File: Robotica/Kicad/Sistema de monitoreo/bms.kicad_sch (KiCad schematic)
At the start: 3 parts, among them J2 TP4056

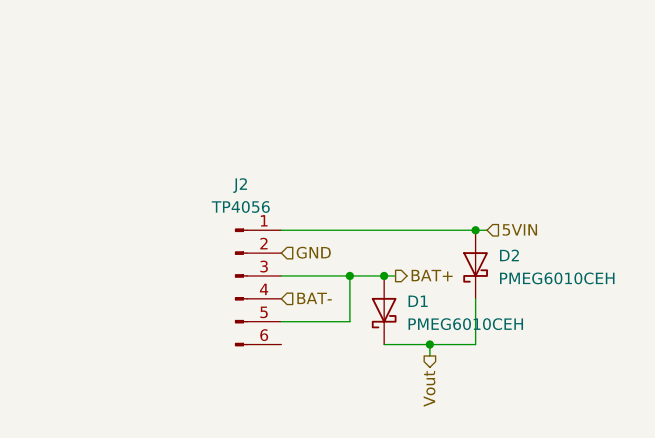
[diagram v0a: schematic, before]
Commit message: Organizacion de esquematicos de robotica
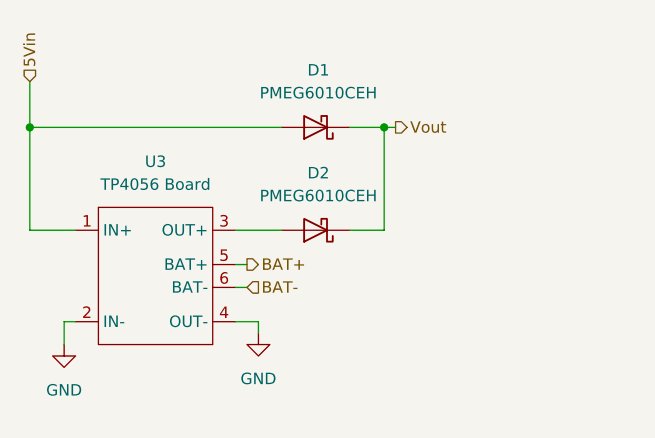
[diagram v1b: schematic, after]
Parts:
- removed J2: TP4056, Connector_PinHeader_2.54mm:PinHeader_1x06_P2.54mm_Vertical, symbol Connector:Conn_01x06_Pin
- added U3: TP4056 Board, Custom board:TP4056 Board, symbol Custom board:TP4056_Board
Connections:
- net BAT+: now also U3.5 (BAT+); no longer D1.2 (A)
- net BAT-: now also U3.6 (BAT-)
- net GND: now also U3.2 (IN-), U3.4 (OUT-)
- net 5VIN: no longer names the net of D2.2 (A)
- net 5VIN: now also U3.3 (OUT+)
- new net 5Vin: D1.2 (A), U3.1 (IN+)
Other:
- moved on the sheet: D1, D2
